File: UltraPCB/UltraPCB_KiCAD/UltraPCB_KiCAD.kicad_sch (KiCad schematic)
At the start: 45 parts, among them J1 USB_C_Receptacle_PowerOnly_6P, J2 Conn_01x04_Pin, Q1 IRLML6401, Q2 IRLML6401, Q3 IRLML6401, Q4 IRLML6401, Q5 IRLML6401, Q6 IRLML6244, SW1 SW_Push, SW2 SW_Push, U2 LM3670MF, U3 LTC-4627JD, U4 STM32F030K6Tx

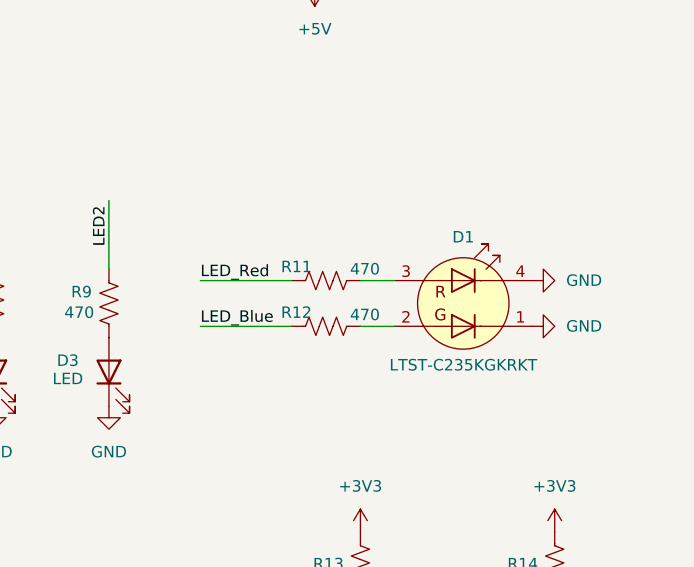
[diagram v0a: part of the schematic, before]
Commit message: New components
D1, SW1-2 changed. Mounting pads added. Minor improvements.
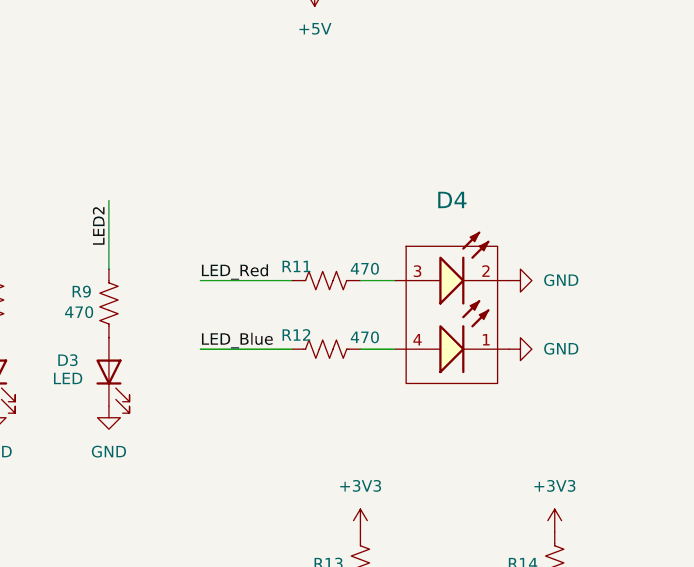
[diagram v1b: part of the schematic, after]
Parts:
- removed D1: LTST-C235KGKRKT, LED_SMD:LED_LiteOn_LTST-C235KGKRKT, symbol LED:LTST-C235KGKRKT
- added D4: Red & Blue, 120°, WL-SBRW_1205_reverse mount, symbol Library:156125RB73000
- SW1, SW2: footprint Button_Switch_SMD:SW_MEC_5GSH9 -> Button_Switch_SMD:SW_SPST_Omron_B3FS-100xP
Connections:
- net GND: now also D4.1 (K), D4.2 (K)
- net at R11.2: now also D4.3 (A)
- net at R12.2: now also D4.4 (A)
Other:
- moved on the sheet: R12

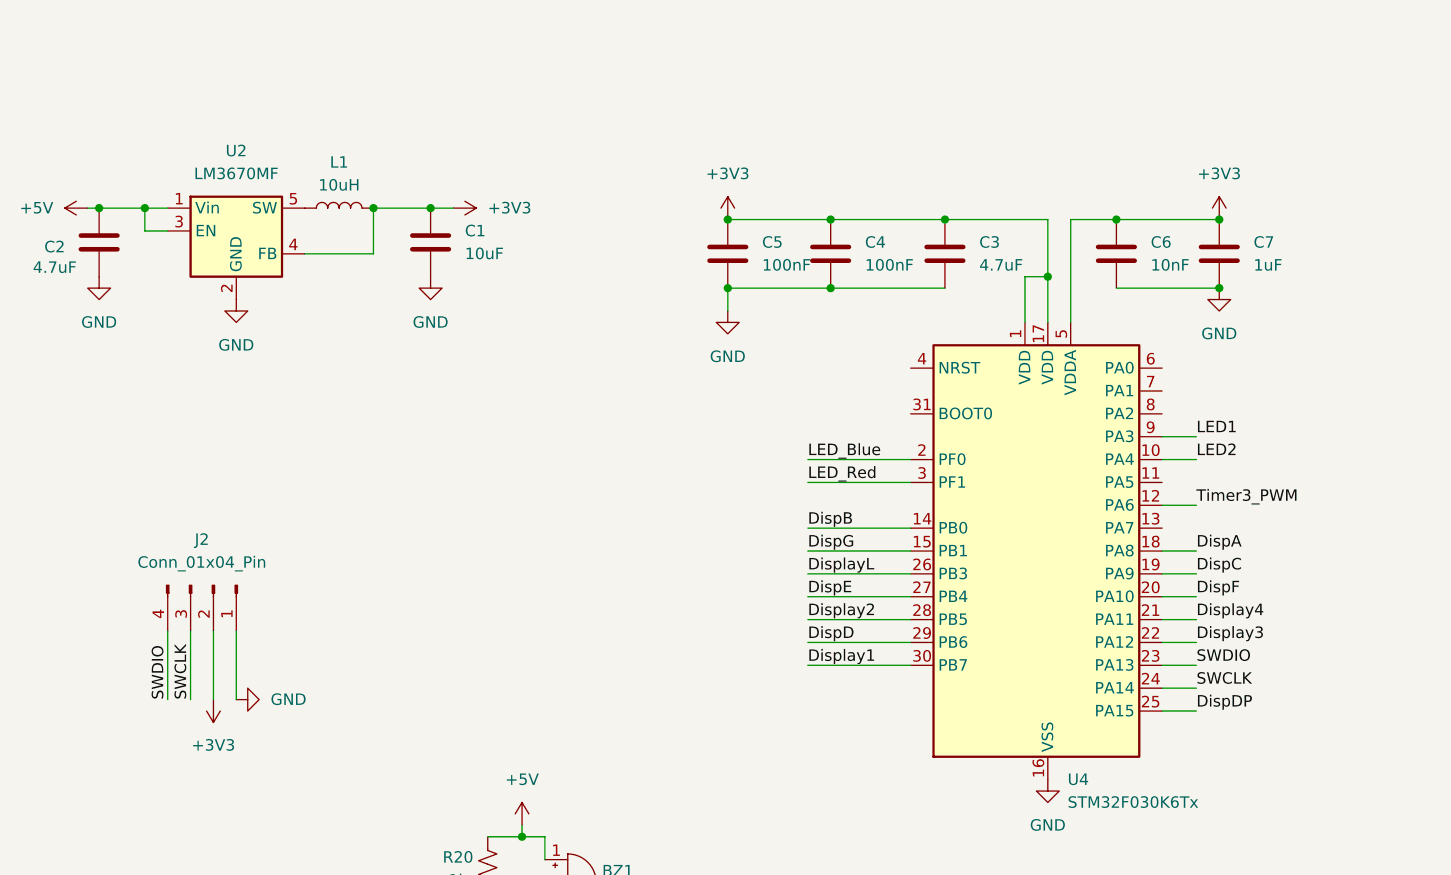
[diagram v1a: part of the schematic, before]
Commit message: Production ready v1.0
Added production files. Components now have mouser part numbers. 7seg display was upside down so it was corrected. All production ready.
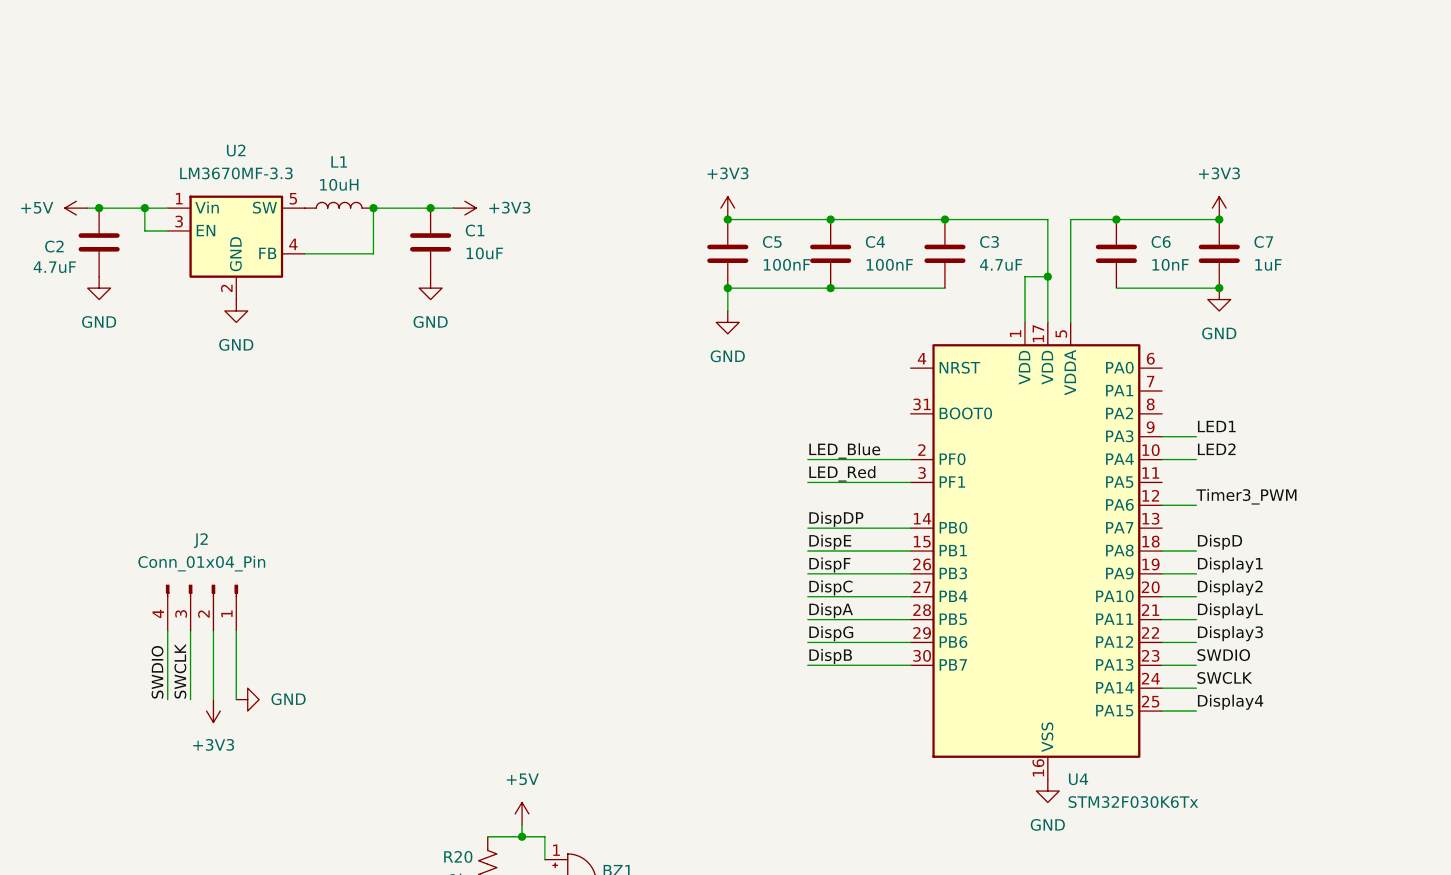
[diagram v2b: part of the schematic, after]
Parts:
- BZ1: Supplier1 (none) -> Mouser; SupplierPartNumber1 (none) -> 490-CPT-9019S-SMT-TR
- C1: Supplier1 (none) -> Mouser; SupplierPartNumber1 (none) -> 81-GRM188R60J106KE7D
- C2, C3: Supplier1 (none) -> Mouser; SupplierPartNumber1 (none) -> 81-GRM185C80J475ME1D
- C4, C5: Supplier1 (none) -> Mouser; SupplierPartNumber1 (none) -> 81-GCJ188R71C104MA1D
- C6: Supplier1 (none) -> Mouser; SupplierPartNumber1 (none) -> 81-GCJ188R71E103KA1D
- C7: Supplier1 (none) -> Mouser; SupplierPartNumber1 (none) -> 81-GRM39R105K10
- D2, D3: Supplier1 (none) -> Mouser; SupplierPartNumber1 (none) -> 710-150080AS75000
- D4: Supplier1 (none) -> Mouser; SupplierPartNumber1 (none) -> 710-156125RB73000
- J1: Supplier1 (none) -> Mouser; SupplierPartNumber1 (none) -> 179-UJCHGSMT2P6TR
- J2: Supplier1 (none) -> Mouser; SupplierPartNumber1 (none) -> 855-M20-8770446
- L1: Supplier1 (none) -> Mouser; SupplierPartNumber1 (none) -> 963-CBMF1608T100K
- Q1, Q2, Q3, Q4, Q5: Supplier1 (none) -> Mouser; SupplierPartNumber1 (none) -> 942-IRLML6401TRPBF
- Q6: Supplier1 (none) -> Mouser; SupplierPartNumber1 (none) -> 942-IRLML6244TRPBF
- R1, R10, R11, R12, R2, R3, R4, R5, R6, R7, R8, R9: Supplier1 (none) -> Mouser; SupplierPartNumber1 (none) -> 603-AC0603FR-7W470RL
- R13, R14, R20: Supplier1 (none) -> Mouser; SupplierPartNumber1 (none) -> 603-AC0603FR-7W1KL
- R15, R16, R17, R18, R19: Supplier1 (none) -> Mouser; SupplierPartNumber1 (none) -> 603-RC0603FR-7W10KL
- SW1, SW2: Supplier1 (none) -> Mouser; SupplierPartNumber1 (none) -> 653-B3FS-1000
- U2: value LM3670MF -> LM3670MF-3.3; Supplier1 (none) -> Mouser; SupplierPartNumber1 (none) -> 926-LM3670MF33NOPB
- U3: Supplier1 (none) -> Mouser; SupplierPartNumber1 (none) -> 859-LTC-4627JD
- U4: Supplier1 (none) -> Mouser; SupplierPartNumber1 (none) -> 511-STM32F030K6T6TR
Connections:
- net DispA: now also U4.28 (PB5); no longer U4.18 (PA8)
- net DispB: now also U4.30 (PB7); no longer U4.14 (PB0)
- net DispC: now also U4.27 (PB4); no longer U4.19 (PA9)
- net DispD: now also U4.18 (PA8); no longer U4.29 (PB6)
- net DispDP: now also U4.14 (PB0); no longer U4.25 (PA15)
- net DispE: now also U4.15 (PB1); no longer U4.27 (PB4)
- net DispF: now also U4.26 (PB3); no longer U4.20 (PA10)
- net DispG: now also U4.29 (PB6); no longer U4.15 (PB1)
- net Display1: now also U4.19 (PA9); no longer U4.30 (PB7)
- net Display2: now also U4.20 (PA10); no longer U4.28 (PB5)
- net Display4: now also U4.25 (PA15); no longer U4.21 (PA11)
- net DisplayL: now also U4.21 (PA11); no longer U4.26 (PB3)

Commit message: Documentation added
PDF and interactive html bom added
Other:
- title: (none) -> UltraPCB
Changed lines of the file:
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@@
 	(generator_version "8.0")
 	(paper "A4")
+	(title_block
+		(title "UltraPCB")
+		(date "2024-10-23")
+		(rev "1.0")
+		(comment 1 "github.com/juamonsan/UltraTimer")
+		(comment 2 "All units in mm")
+	)
 	(junction
 		(at 114.3 93.98)

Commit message: Revision 1.2
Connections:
- net SW1_IN: now also U4.13 (PA7)
- net SW2_IN: now also U4.11 (PA5)
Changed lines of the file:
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@@
 	(title_block
 		(title "UltraPCB")
-		(date "2024-10-25")
-		(rev "1.1")
+		(date "2025-02-13")
+		(rev "1.2")
 		(comment 1 "github.com/juamonsan/UltraTimer")
 		(comment 2 "All units in mm")
@@
 	(wire
 		(pts
+			(xy 154.94 128.27) (xy 151.13 128.27)
+		)
+		(stroke
+			(width 0)
+			(type default)
+		)
+	)
+	(wire
+		(pts
 			(xy 111.76 58.42) (xy 115.57 58.42)
 		)
@@
 		(pts
 			(xy 63.5 97.79) (xy 63.5 92.71)
+		)
+		(stroke
+			(width 0)
+			(type default)
+		)
+	)
+	(wire
+		(pts
+			(xy 154.94 123.19) (xy 151.13 123.19)
 		)
 		(stroke
@@
 	(label "SWCLK"
 		(at 154.94 146.05 0)
-		(fields_autoplaced yes)
 		(effects
 			(font
@@
 	(label "Display2"
 		(at 154.94 135.89 0)
-		(fields_autoplaced yes)
 		(effects
 			(font
@@
 	(label "CA4"
 		(at 252.73 43.18 0)
-		(fields_autoplaced yes)
 		(effects
 			(font
@@
 	(label "SWCLK"
 		(at 43.18 147.32 90)
-		(fields_autoplaced yes)
 		(effects
 			(font
@@
 	(label "DispD"
 		(at 93.98 48.26 0)
-		(fields_autoplaced yes)
 		(effects
 			(font
@@
 	(label "CAL"
 		(at 234.95 63.5 0)
-		(fields_autoplaced yes)
 		(effects
 			(font
@@
 	(label "Display1"
 		(at 185.42 29.21 0)
-		(fields_autoplaced yes)
 		(effects
 			(font
@@
 	(label "Display1"
 		(at 154.94 133.35 0)
-		(fields_autoplaced yes)
 		(effects
 			(font
@@
 	(label "Display3"
 		(at 185.42 48.26 0)
-		(fields_autoplaced yes)
 		(effects
 			(font
@@
 	(label "DispC"
 		(at 93.98 43.18 0)
-		(fields_autoplaced yes)
 		(effects
 			(font
@@
 	(label "DispF"
 		(at 111.76 133.35 0)
-		(fields_autoplaced yes)
 		(effects
 			(font
@@
 	(label "CA3"
 		(at 209.55 43.18 0)
-		(fields_autoplaced yes)
 		(effects
 			(font
@@
 	(label "CA1"
 		(at 156.21 53.34 0)
-		(fields_autoplaced yes)
 		(effects
 			(font
@@
 	(label "DisplayL"
 		(at 210.82 68.58 0)
-		(fields_autoplaced yes)
 		(effects
 			(font
@@
 	(label "DispE"
 		(at 111.76 130.81 0)
-		(fields_autoplaced yes)
 		(effects
 			(font
@@
 	(label "DispG"
 		(at 93.98 62.23 0)
-		(fields_autoplaced yes)
 		(effects
 			(font
@@
 	(label "LED_Blue"
 		(at 111.76 120.65 0)
-		(fields_autoplaced yes)
 		(effects
 			(font
@@
 	(label "CAL"
 		(at 156.21 63.5 0)
-		(fields_autoplaced yes)
+		(effects
+			(font
+				(size 1.27 1.27)
+			)
+			(justify left bottom)
+		)
+	)
+	(label "SW1_IN"
+		(at 154.94 128.27 0)
 		(effects
 			(font
@@
 	(label "SW1_IN"
 		(at 226.06 142.24 0)
-		(fields_autoplaced yes)
 		(effects
 			(font
@@
 	(label "SWDIO"
 		(at 154.94 143.51 0)
-		(fields_autoplaced yes)
 		(effects
 			(font
@@
 	(label "CA2"
 		(at 252.73 25.4 0)
-		(fields_autoplaced yes)
 		(effects
 			(font
@@
 	(label "CA4"
 		(at 156.21 60.96 0)
-		(fields_autoplaced yes)
 		(effects
 			(font
@@
 	(label "Display3"
 		(at 154.94 140.97 0)
-		(fields_autoplaced yes)
 		(effects
 			(font
@@
 	(label "Display4"
 		(at 154.94 148.59 0)
-		(fields_autoplaced yes)
 		(effects
 			(font
@@
 	(label "DispB"
 		(at 111.76 143.51 0)
-		(fields_autoplaced yes)
 		(effects
 			(font
@@
 	(label "SW2_IN"
 		(at 247.65 142.24 0)
-		(fields_autoplaced yes)
+		(effects
+			(font
+				(size 1.27 1.27)
+			)
+			(justify left bottom)
+		)
+	)
+	(label "SW2_IN"
+		(at 154.94 123.19 0)
 		(effects
 			(font
@@
 	(label "DispA"
 		(at 111.76 138.43 0)
-		(fields_autoplaced yes)
 		(effects
 			(font
@@
 	(label "LED1"
 		(at 199.39 102.87 90)
-		(fields_autoplaced yes)
 		(effects
 			(font
@@
 	(label "CA1"
 		(at 209.55 24.13 0)
-		(fields_autoplaced yes)
 		(effects
 			(font
@@
 	(label "DispDP"
 		(at 92.71 66.04 0)
-		(fields_autoplaced yes)
 		(effects
 			(font
@@
 	(label "CA3"
 		(at 156.21 58.42 0)
-		(fields_autoplaced yes)
 		(effects
 			(font
@@
 	(label "DispC"
 		(at 111.76 135.89 0)
-		(fields_autoplaced yes)
 		(effects
 			(font
@@
 	(label "LED_Blue"
 		(at 222.25 114.3 0)
-		(fields_autoplaced yes)
 		(effects
 			(font
@@
 	(label "Timer3_PWM"
 		(at 154.94 125.73 0)
-		(fields_autoplaced yes)
 		(effects
 			(font
@@
 	(label "LED_Red"
 		(at 111.76 123.19 0)
-		(fields_autoplaced yes)
 		(effects
 			(font
@@
 	(label "DispB"
 		(at 93.98 38.1 0)
-		(fields_autoplaced yes)
 		(effects
 			(font
@@
 	(label "DisplayL"
 		(at 154.94 138.43 0)
-		(fields_autoplaced yes)
 		(effects
 			(font
@@
 	(label "DispG"
 		(at 111.76 140.97 0)
-		(fields_autoplaced yes)
 		(effects
 			(font
@@
 	(label "DispDP"
 		(at 111.76 128.27 0)
-		(fields_autoplaced yes)
 		(effects
 			(font
@@
 	(label "Display2"
 		(at 228.6 30.48 0)
-		(fields_autoplaced yes)
 		(effects
 			(font
@@
 	(label "SWDIO"
 		(at 40.64 147.32 90)
-		(fields_autoplaced yes)
 		(effects
 			(font
@@
 	(label "LED1"
 		(at 154.94 118.11 0)
-		(fields_autoplaced yes)
 		(effects
 			(font
@@
 	(label "LED2"
 		(at 154.94 120.65 0)
-		(fields_autoplaced yes)
 		(effects
 			(font
@@
 	(label "DispF"
 		(at 93.98 57.15 0)
-		(fields_autoplaced yes)
 		(effects
 			(font
@@
 	(label "Display4"
 		(at 228.6 48.26 0)
-		(fields_autoplaced yes)
 		(effects
 			(font
@@
 	(label "DispE"
 		(at 93.98 53.34 0)
-		(fields_autoplaced yes)
 		(effects
 			(font
@@
 	(label "DispA"
 		(at 93.98 33.02 0)
-		(fields_autoplaced yes)
 		(effects
 			(font
@@
 	(label "DispD"
 		(at 154.94 130.81 0)
-		(fields_autoplaced yes)
 		(effects
 			(font
@@
 	(label "LED2"
 		(at 212.09 102.87 90)
-		(fields_autoplaced yes)
 		(effects
 			(font
@@
 	(label "CA2"
 		(at 156.21 55.88 0)
-		(fields_autoplaced yes)
 		(effects
 			(font
@@
 	(label "LED_Red"
 		(at 222.25 106.68 0)
-		(fields_autoplaced yes)
 		(effects
 			(font
@@
 	(label "Timer3_PWM"
 		(at 59.69 176.53 0)
-		(fields_autoplaced yes)
-		(effects
-			(font
+		(effects
+			(font

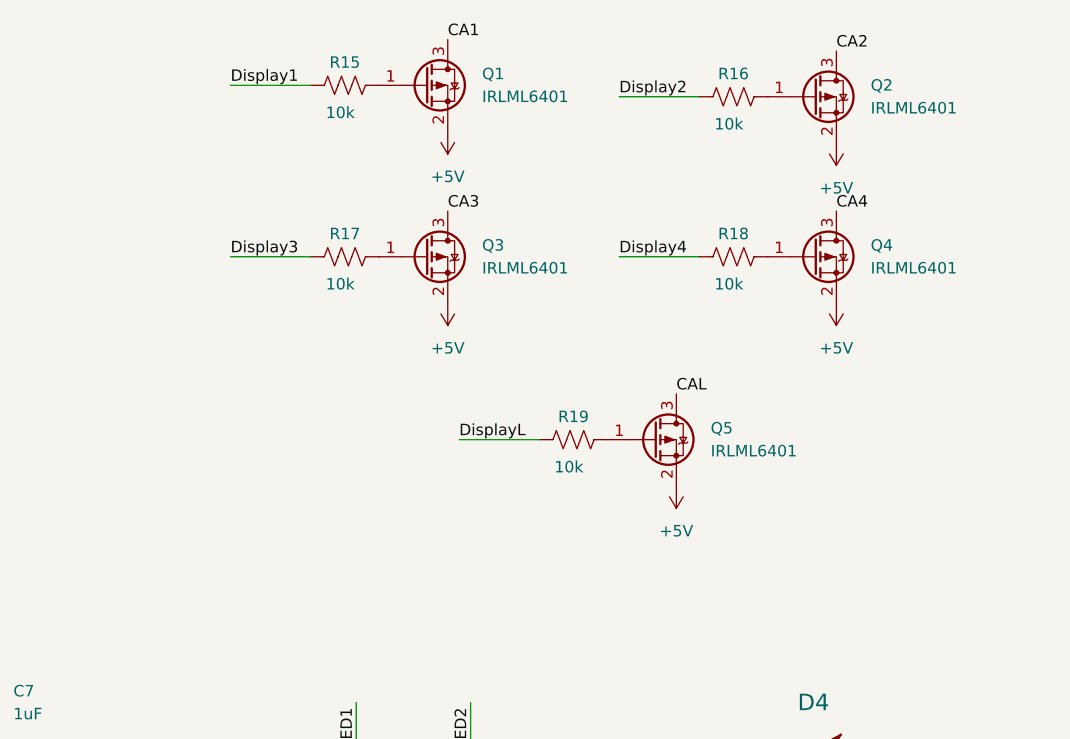
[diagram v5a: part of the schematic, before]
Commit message: Q1-5 replaced
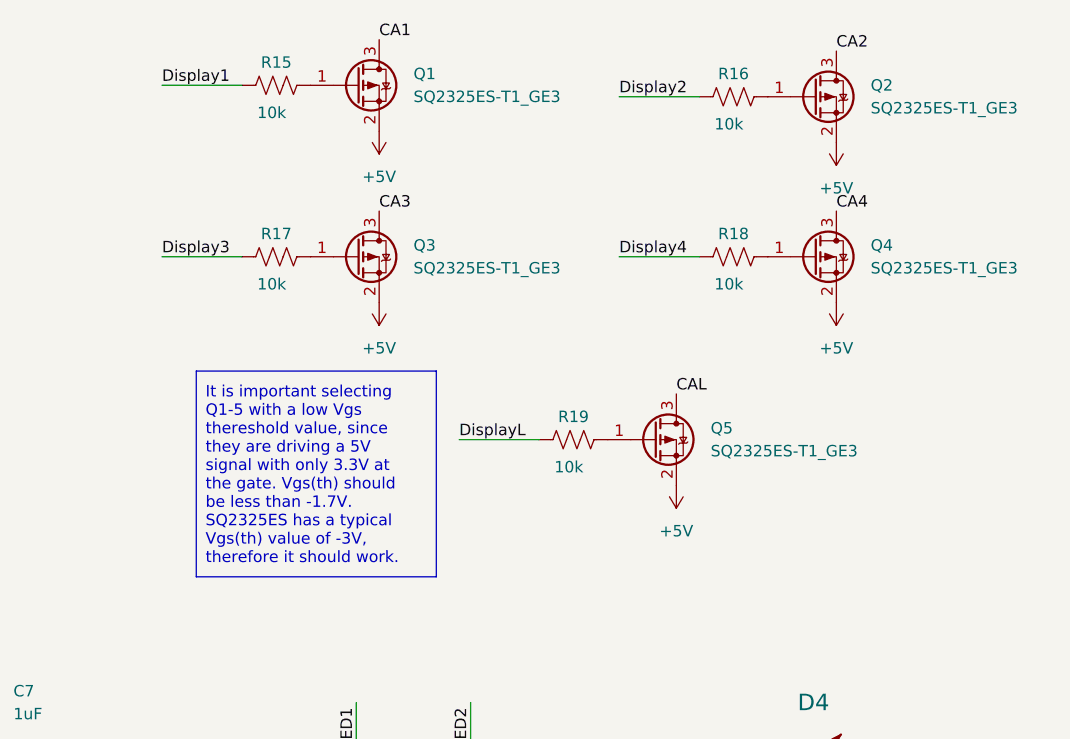
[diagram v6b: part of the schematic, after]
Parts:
- Q1, Q2, Q3, Q4, Q5: value IRLML6401 -> SQ2325ES-T1_GE3; symbol Transistor_FET:IRLML6401 -> Library:SQ2325ES-T1_GE3; SupplierPartNumber1 942-IRLML6401TRPBF -> 78-SQ2325ES-T1_GE3
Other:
- moved on the sheet: Q1, Q3, R15, R17
